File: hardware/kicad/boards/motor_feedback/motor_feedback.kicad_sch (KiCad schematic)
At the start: 10 parts, among them J1 Screw_Terminal_01x03, J3 Screw_Terminal_01x03, U1 IL300, U11 MCP601, U9 MCP601

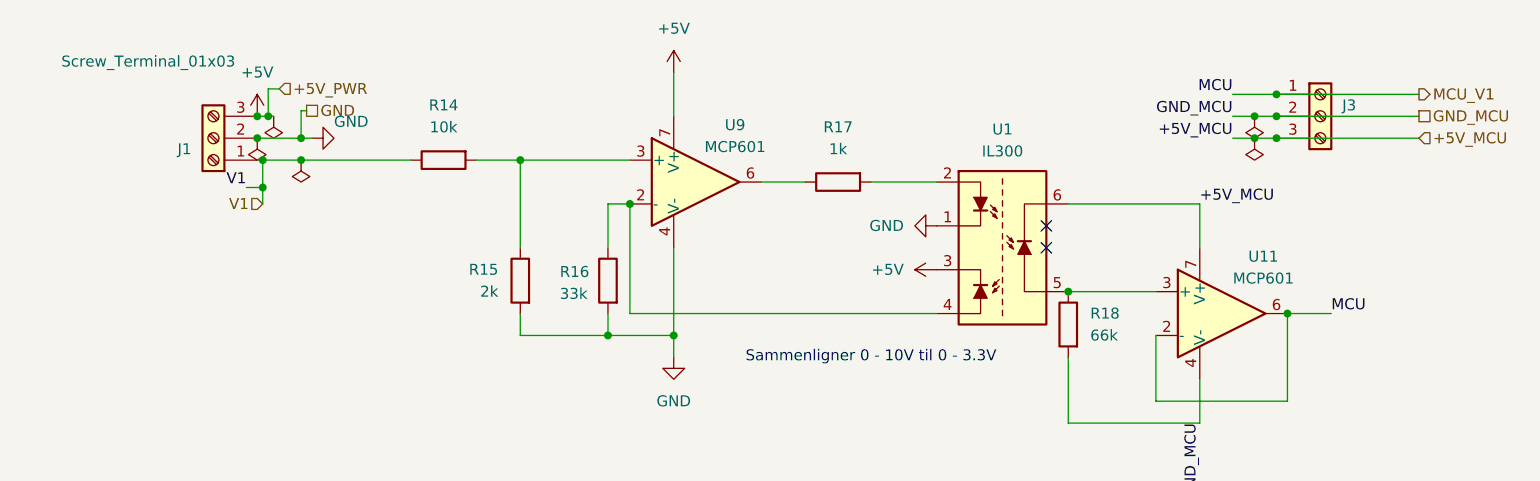
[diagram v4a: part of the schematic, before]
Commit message: system: single edge-connector set + integrated board
- delete 22 redundant board-level I/O connectors (J201-207, J301-302,
  J401-404, J501-504, J601-605); on the monolithic board these are internal
  board-to-board nets (now copper traces) or duplicates of the top-level edge
  set. Nets carried by the hierarchical sheet pins; netlist re-verified.
- C212: real capacitor footprint, + on V1 (was a swap terminal)
- motor_feedback MCU-side powered from +5V_PWR (merged +5V_MCU)
- footprints assigned to all top-level connectors/probes (J_*, TP, R_STAR)
- system.kicad_pcb: integrated board pulled via Update-PCB-from-Schematic
- placement guide (PNG + PDF) + generator/patch scripts
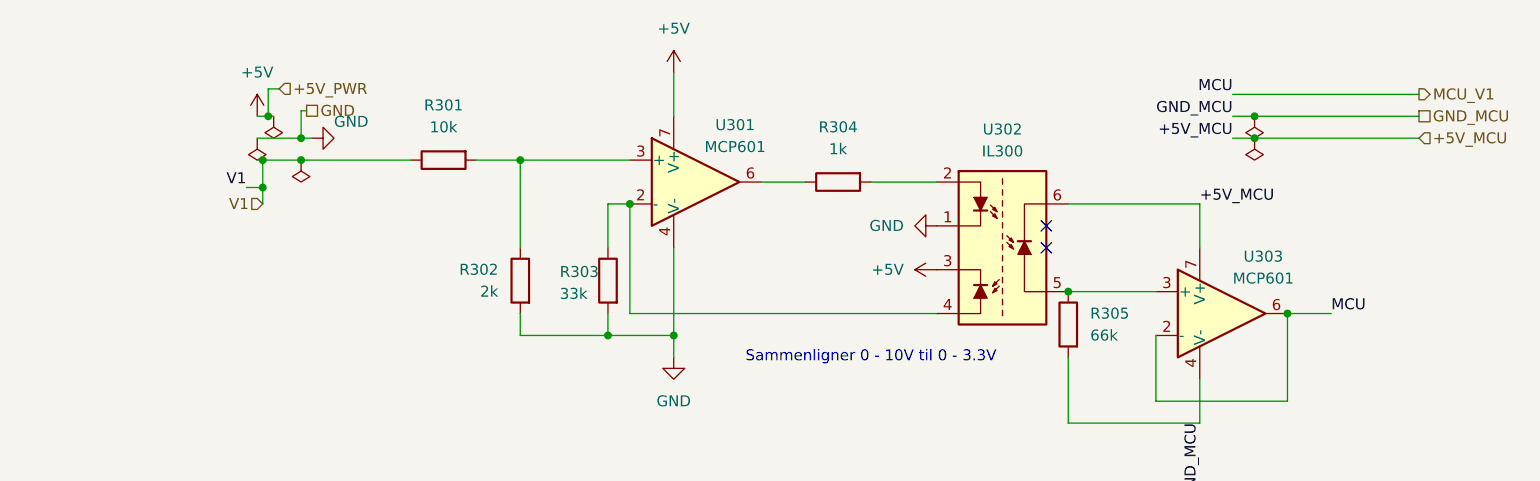
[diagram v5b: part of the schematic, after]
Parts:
- removed J1, J3: Screw_Terminal_01x03, TerminalBlock:TerminalBlock_bornier-3_P5.08mm, symbol Connector:Screw_Terminal_01x03
- renumbered R14 to R301, R15 to R302, R16 to R303, R17 to R304, R18 to R305, U9 to U301, U1 to U302, U11 to U303
